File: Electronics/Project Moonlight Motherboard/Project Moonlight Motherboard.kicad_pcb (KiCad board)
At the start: 4 copper layers, 105 x 56 mm, 41 parts, among them M1 AO3400A, M2 AO3400A, M3 AO3400A, U2 TMC2209_SILENTSTEPSTICK, U3 TMC2209_SILENTSTEPSTICK, U4 TMC2209_SILENTSTEPSTICK, U5 TMC2209_SILENTSTEPSTICK, U6 STM32H563VITx

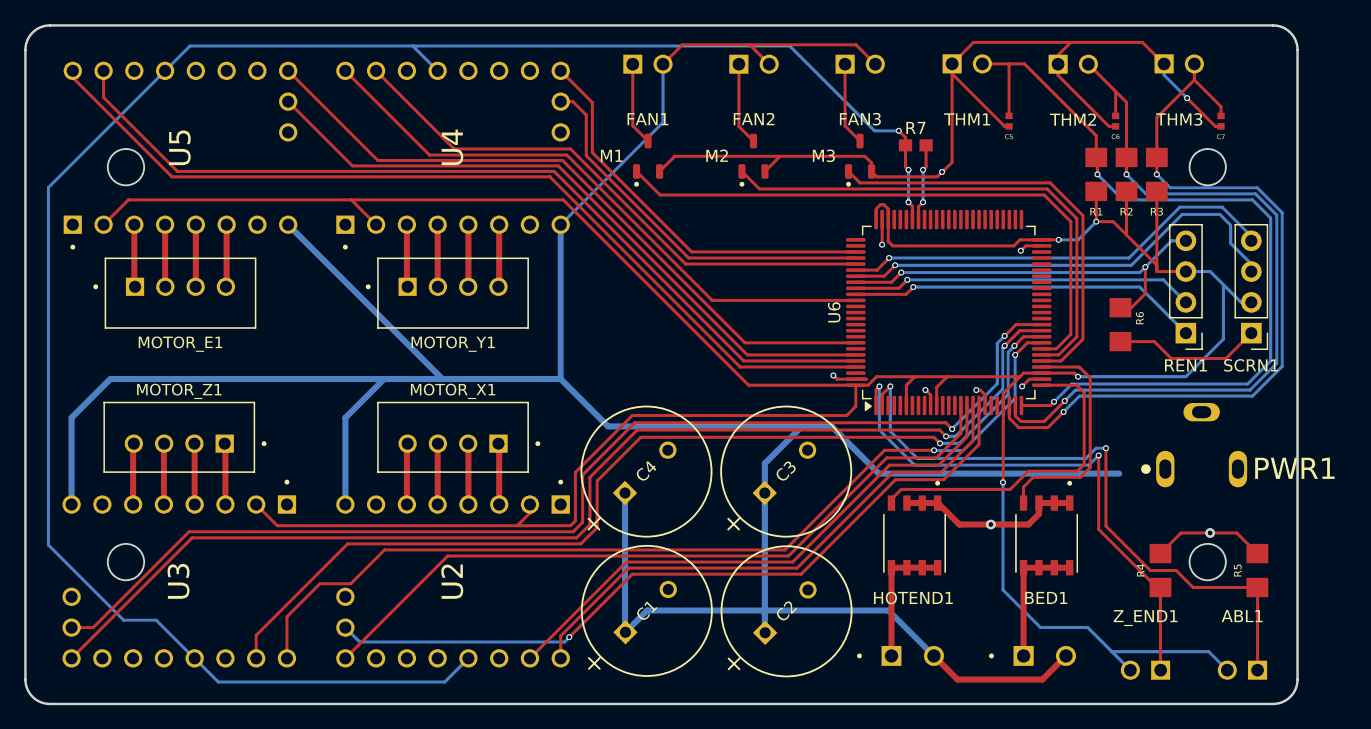
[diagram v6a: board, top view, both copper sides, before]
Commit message: added debug header and programming USB port, tidied up silkscreen
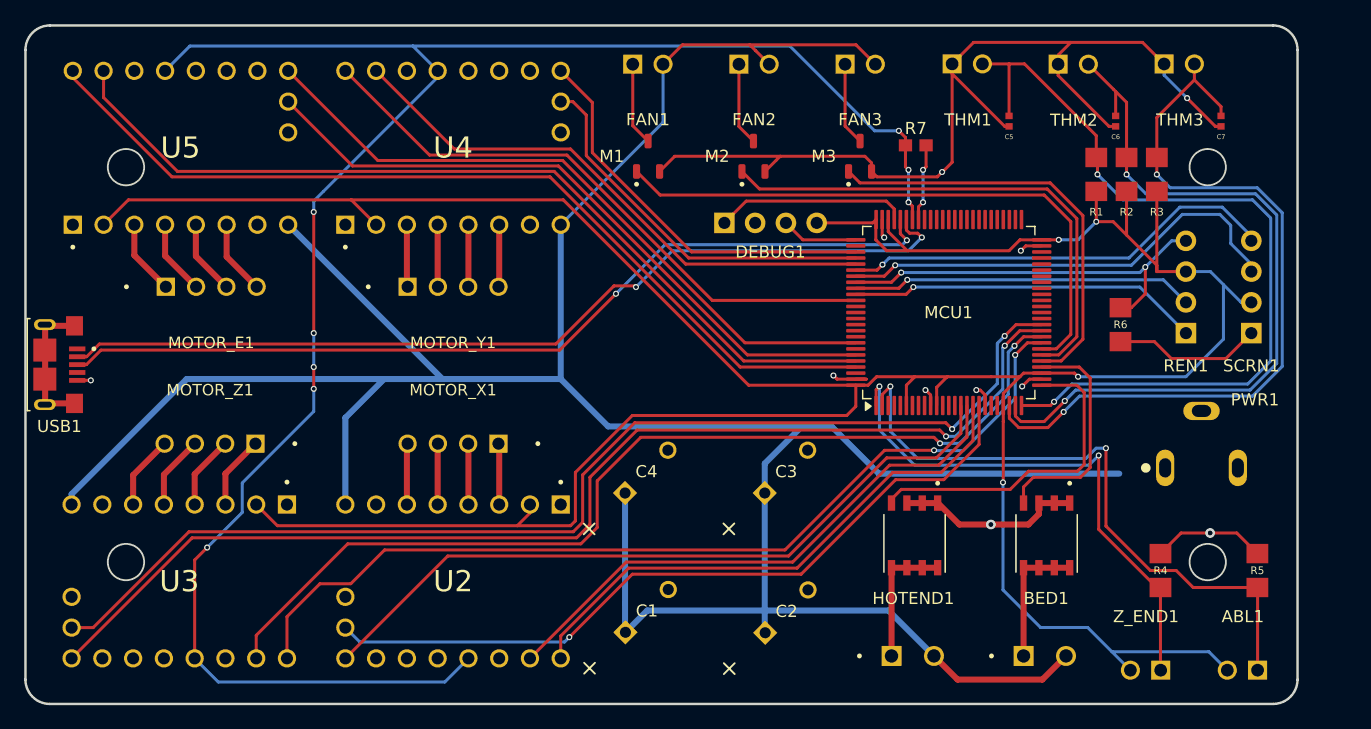
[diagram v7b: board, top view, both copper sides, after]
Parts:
- added DEBUG1: Conn_01x04_Pin, Connector_PinHeader_2.54mm:PinHeader_1x04_P2.54mm_Vertical, F.Cu at (158.1, 88.3)
- added USB1: 10118193-0001LF, 10118193-0001LF:AMPHENOL_10118193-0001LF, F.Cu at (102.0, 100.0)
- moved MOTOR_Z1 2.54 mm to (115.6, 106.0)
- moved MOTOR_E1 2.54 mm to (115.7, 94.1)
- moved PWR1 0.10 mm to (201.0, 108.5)
- renumbered U6 to MCU1
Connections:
- MCU1 pad 70: unconnected-(U6-PA11-Pad70) -> USB_DM
- MCU1 pad 71: unconnected-(U6-PA12-Pad71) -> USB_DP
- MCU1 pad 72: unconnected-(U6-PA13(JTMS-Pad72) -> SWDIO
- MCU1 pad 76: unconnected-(U6-PA14(JTCK-Pad76) -> SWCLK
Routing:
- net USB_DM: track 0.00 -> 76.3 mm, vias 0 -> 2
- net USB_DP: track 0.00 -> 74.7 mm, vias 0 -> 2
- net SWDIO: track 0.00 -> 15.9 mm
- net Net-(USB1-SHIELD-PadS1): track 0.00 -> 11.6 mm
- net +3V3: track 268.0 -> 274.5 mm
- net SWCLK: track 0.00 -> 6.35 mm
- net VCC: track 250.9 -> 247.2 mm
- net UART_RX: track 158.3 -> 156.0 mm, vias 3 -> 8
- net Net-(U3-M2A): track 5.03 -> 6.08 mm
- net Net-(U3-M2B): track 5.05 -> 6.10 mm
- net Net-(U5-M1A): track 5.13 -> 6.18 mm
- net Net-(U5-M1B): track 5.15 -> 6.20 mm
- net Net-(U5-M2A): track 5.13 -> 6.17 mm
- net Net-(U3-M1A): track 5.03 -> 6.07 mm
- net Net-(U3-M1B): track 5.05 -> 6.05 mm
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
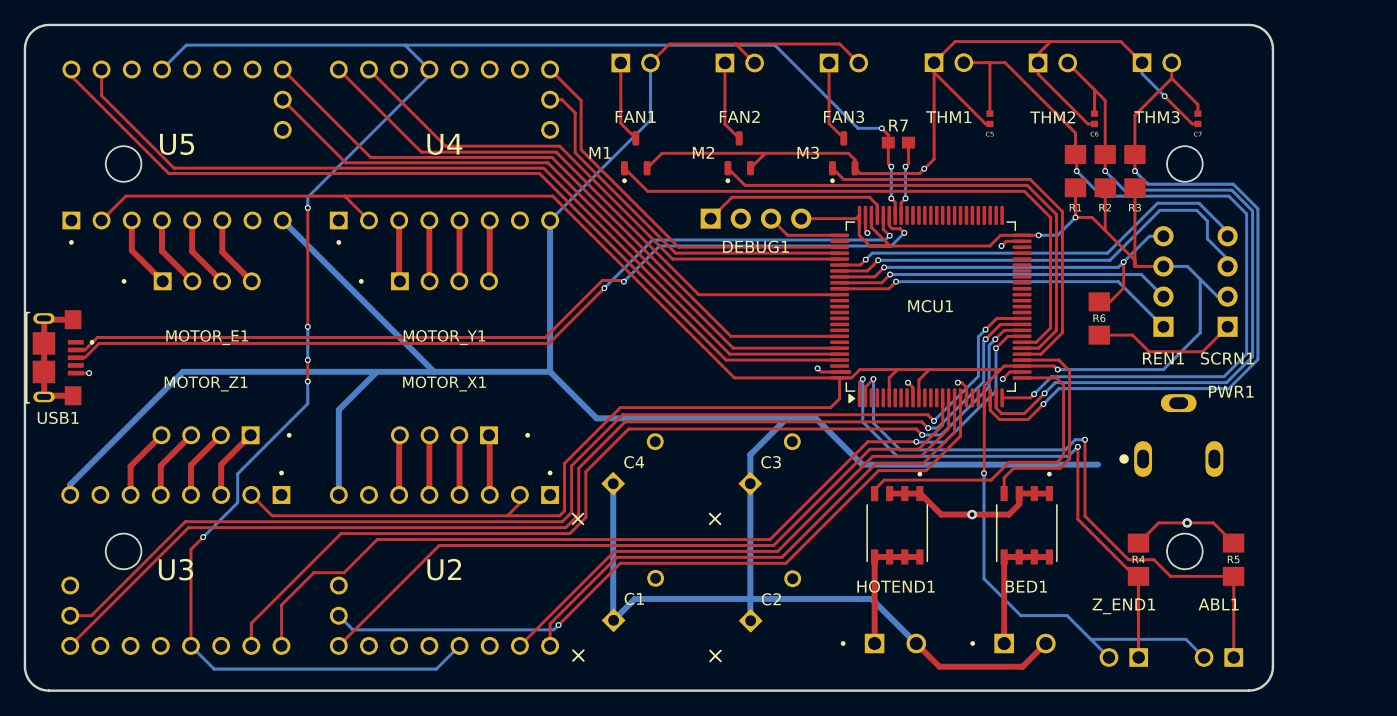
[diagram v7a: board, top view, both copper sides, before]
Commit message: added voltage reg, fuse, resistors, etc
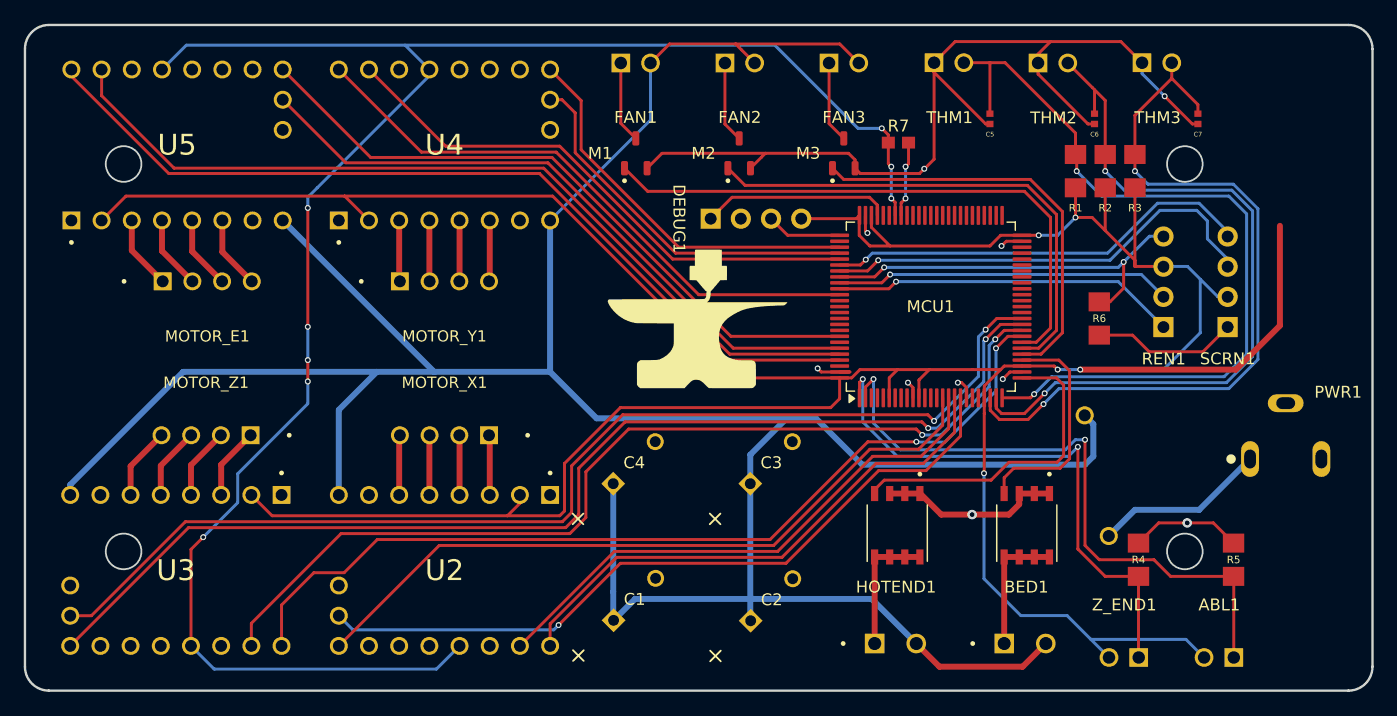
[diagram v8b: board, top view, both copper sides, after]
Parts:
- removed USB1: 10118193-0001LF, 10118193-0001LF:AMPHENOL_10118193-0001LF
- added F1: RUEF900, RUEF900:FUSRR1015W81L2410T300H2900, B.Cu at (190.6, 109.9)
- added G***: LOGO, LOGO, F.Cu at (156.9, 97.8)
- added G***: LOGO, LOGO, B.Cu at (159.4, 96.9)
- DEBUG1, REN1, SCRN1: footprint Connector_PinHeader_2.54mm:PinHeader_1x04_P2.54mm_Vertical -> PinHeader:PinHeader_1x04_P2.54mm_Vertical
- moved PWR1 9.00 mm to (210.0, 108.5)
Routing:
- net USB_DM: track 76.3 -> 0.00 mm, vias 2 -> 0
- net USB_DP: track 74.7 -> 0.00 mm, vias 2 -> 0
- net +3V3: track 274.5 -> 301.3 mm, vias 4 -> 5
- net Net-(F1-Pad1): track 0.00 -> 14.6 mm
- net Net-(USB1-SHIELD-PadS1): track 11.6 -> 0.00 mm
- net VCC: track 247.2 -> 250.8 mm
- net Z_END: track 44.9 -> 46.4 mm
- net ABL: track 52.5 -> 53.9 mm
- net GNDREF: track 130.2 -> 128.9 mm, vias 11 -> 10
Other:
- board size 105 x 56 mm -> 113.4 x 56 mm
